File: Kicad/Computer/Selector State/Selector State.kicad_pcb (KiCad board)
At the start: 2 copper layers, 61 x 61 mm, 73 parts, among them IC1 FAN2558S38X, IC10 74LVC257AD,118, IC11 74LVC257AD,118, IC12 74LVC4245APW,118, IC2 74LVC32APW,118, IC3 74LVC32APW,118, IC4 74VHC595FT, IC5 74LVC2G08DP-Q100H, IC6 SN74ABT245BDBR, IC7 SN74ABT245BDBR, IC8 74ALVC04PW,118, IC9 74ALVC00PW,118, J1 Conn_01x02_Male, J10 Conn_01x02_Male, J11 Conn_01x10_Male, J12 Conn_01x02_Male, J2 Conn_01x12_Male, J3 Conn_01x02_Male, J4 Conn_01x02_Male, J5 Conn_01x12_Male, J6 Conn_01x02_Male, J7 Conn_01x02_Male, J8 Conn_01x10_Male, J9 Conn_01x02_Male

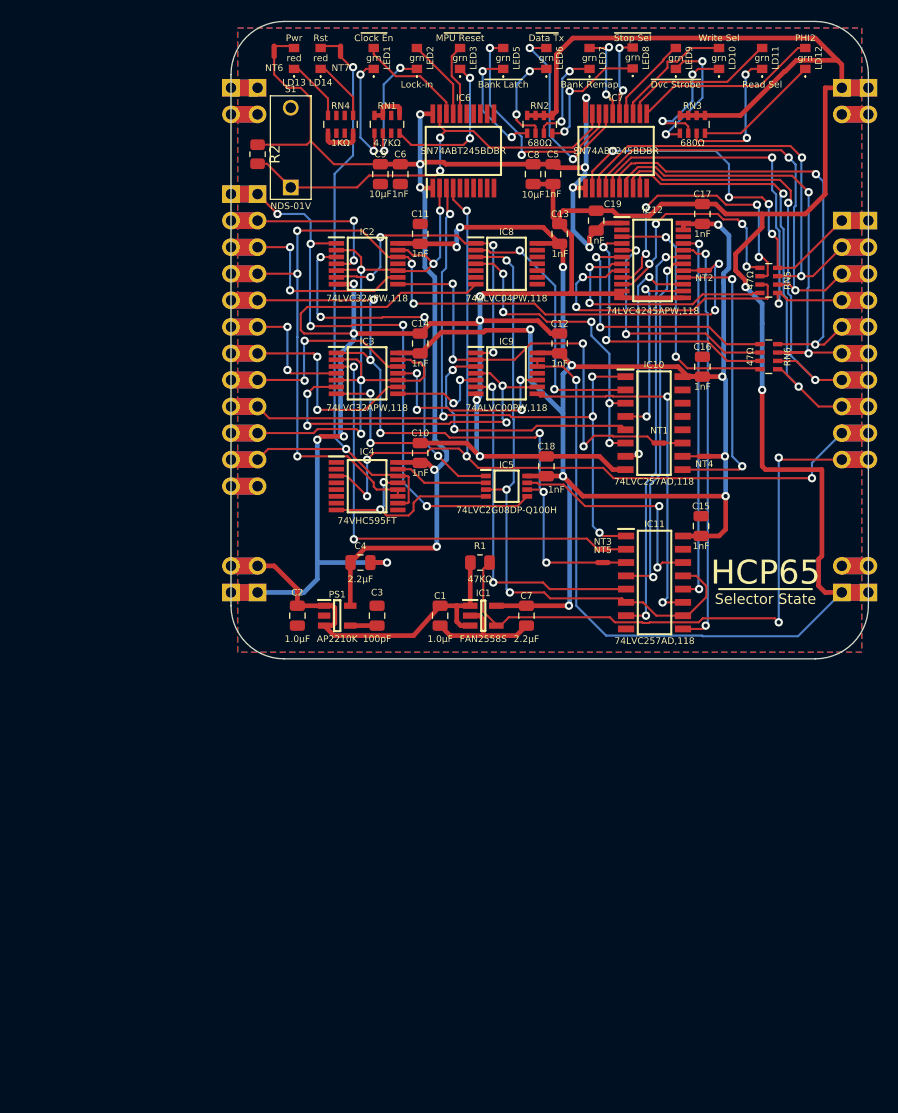
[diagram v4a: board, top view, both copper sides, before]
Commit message: Re-routed Selector State based on new simulation.
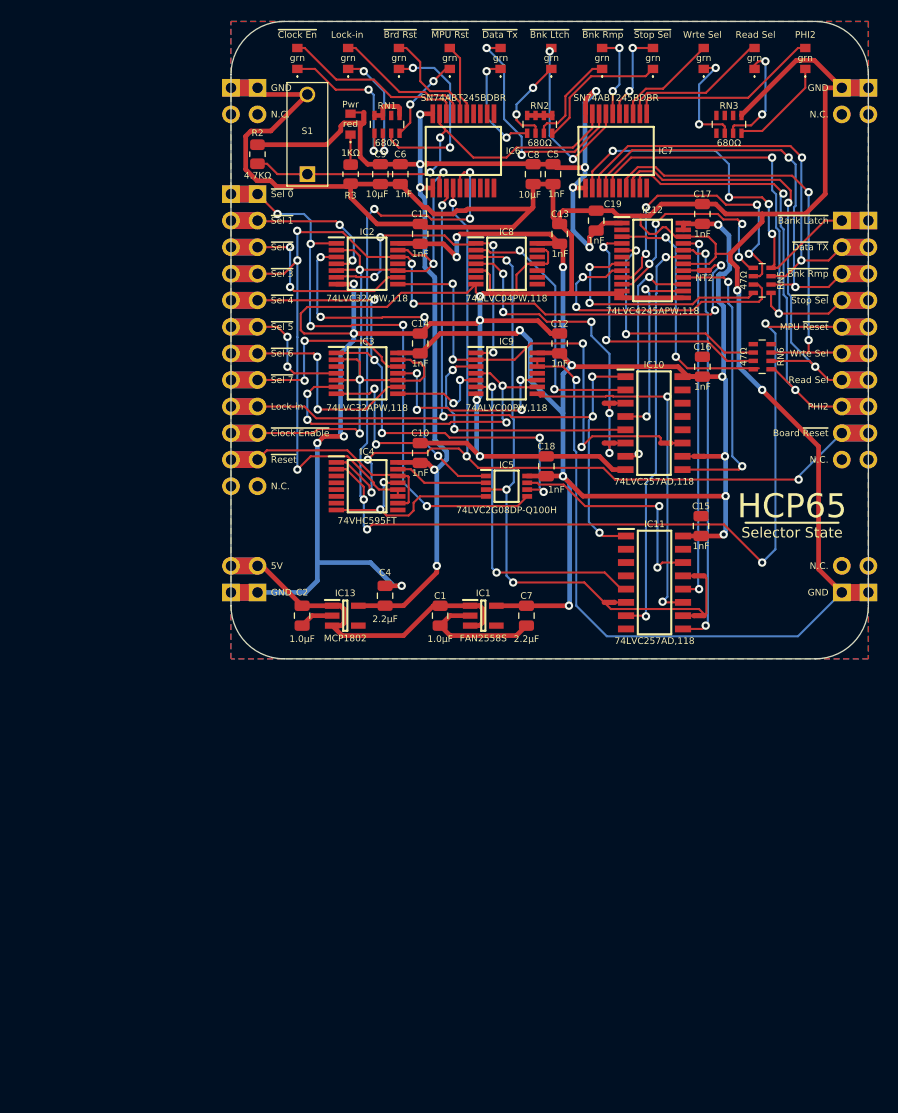
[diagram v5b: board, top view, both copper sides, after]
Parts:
- removed C3: C_Small, Capacitor_SMD:C_0805_2012Metric
- removed LD14: 150224SS73100, SamacSys_Parts:150224SS73100A
- removed LED9: 150224VS73100A, SamacSys_Parts:150224VS73100A
- removed PS1: AP2210K-5.0TRG1, SamacSys_Parts:SOT95P282X130-5N
- removed R1: R_Small, Resistor_SMD:R_0805_2012Metric
- removed RN4: CAY16-102J4LF, SamacSys_Parts:CAY16-J4
- added IC13: MCP1802T-5002I_OT, SamacSys_Parts:SOT95P270X145-5N, F.Cu at (153.2, 93.7)
- added LED4: 150224VS73100A, SamacSys_Parts:150224VS73100A, F.Cu at (163.2, 40.4)
- added NT8: NetTie_2, NetTie:NetTie-2_SMD_Pad0.5mm, F.Cu at (187.0, 93.7)
- added NT9: NetTie_2, NetTie:NetTie-2_SMD_Pad0.5mm, F.Cu at (187.0, 89.9)
- added R3: R_0805, SamacSys_Parts:R_0805, F.Cu at (153.7, 51.4)
- R2: value R_Small -> R_0805; footprint Resistor_SMD:R_0805_2012Metric -> SamacSys_Parts:R_0805
- RN1: value CAY16-472J4LF -> CAY16-681J4LF
- moved NT7 58.6 mm to (178.4, 92.4), turned to 0 degrees
- moved NT3 14.0 mm to (178.4, 73.3)
- moved NT5 11.4 mm to (178.4, 77.2)
- moved NT6 10.7 mm to (154.9, 46.0)
- moved LD13 8.29 mm to (153.7, 46.7)
- moved LED1 7.30 mm to (148.6, 40.4)
- moved LED2 6.57 mm to (153.4, 40.4)
- moved LED3 5.84 mm to (158.3, 40.4)
- moved C4 3.95 mm to (157.0, 91.8), turned to -90 degrees
- moved RN3 3.49 mm to (189.9, 46.7)
- moved S1 2.03 mm to (149.5, 51.4)
- moved LED8 1.94 mm to (182.6, 40.4)
- moved LD10 1.46 mm to (187.5, 40.4)
- moved LED7 1.21 mm to (177.7, 40.4)
- moved LD11 0.73 mm to (192.3, 40.4)
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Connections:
- net /Power LED renamed /Power^{LED}
- net 3V renamed /3.8V
- net Net-(IC6-Pad16) renamed /Board ~{Reset}^{LED}
- net Net-(IC6-Pad17) renamed /MPU Lock-in^{LED}
- net Net-(IC6-Pad18) renamed /~{Clock Enable}^{LED}
- net Net-(IC7-Pad11) renamed /~{PHI2}^{LED}
- net Net-(IC7-Pad12) renamed /Read Selector^{LED}
- net Net-(IC7-Pad13) renamed /Write Selector^{LED}
- net Net-(IC7-Pad15) renamed /~{Stop Selector}^{LED}
- net Net-(IC7-Pad16) renamed /~{Read Bank Remap}^{LED}
- net Net-(IC7-Pad17) renamed /~{Data Transmit}^{LED}
- net Net-(IC7-Pad18) renamed /~{Bank Latch}^{LED}
- C1 pad 1: GND -> /GND
- C10 pad 1: GND -> /GND
- C10 pad 2: 5V -> /5V
- C11 pad 1: GND -> /GND
- C12 pad 1: GND -> /GND
- C13 pad 1: GND -> /GND
- C14 pad 1: GND -> /GND
- C15 pad 1: GND -> /GND
- C16 pad 1: GND -> /GND
- C17 pad 1: GND -> /GND
- C18 pad 1: GND -> /GND
- C19 pad 1: GND -> /GND
- C19 pad 2: 5V -> /5V
- C2 pad 1: GND -> /GND
- C4 pad 1: GND -> /GND
- C4 pad 2: 5V -> /5V
- C5 pad 1: GND -> /GND
- C5 pad 2: 5V -> /5V
- C6 pad 1: GND -> /GND
- C6 pad 2: 5V -> /5V
- C7 pad 1: GND -> /GND
- C8 pad 1: GND -> /GND
- C8 pad 2: 5V -> /5V
- C9 pad 1: GND -> /GND
- C9 pad 2: 5V -> /5V
- IC1 pad 2: GND -> /GND
- IC1 pad 4: /~{Power Error} -> unconnected-(IC1-Pad4)
- IC10 pad 13: GND -> /GND
- IC10 pad 14: GND -> /GND
- IC10 pad 15: GND -> /GND
- IC10 pad 6: /~{Bank Latch}_{2} -> /~{Data Transmit}_{2}
- IC10 pad 8: GND -> /GND
- IC11 pad 13: /Read Selector_{2} -> /~{PHI2}_{2}
- IC11 pad 15: GND -> /GND
- IC11 pad 2: /~{Device Strobe}_{1} -> /GND
- IC11 pad 3: /~{Device Strobe}_{2} -> /GND
- IC11 pad 4: Net-(IC11-Pad4) -> unconnected-(IC11-Pad4)
- IC11 pad 6: /Read Selector_{2} -> /Write Selector_{2}
- IC11 pad 8: GND -> /GND
- IC12 pad 1: 5V -> /5V
- IC12 pad 11: GND -> /GND
- IC12 pad 12: GND -> /GND
- IC12 pad 13: GND -> /GND
- IC12 pad 18: Net-(IC11-Pad4) -> /GND
- IC12 pad 2: GND -> /GND
- IC12 pad 22: GND -> /GND
- IC12 pad 6: Net-(IC12-Pad6) -> unconnected-(IC12-Pad6)
- IC2 pad 11: /Select 3 ^{AND} Enable -> unconnected-(IC2-Pad11)
- IC2 pad 7: GND -> /GND
- IC3 pad 3: /Select 4 ^{AND} Enable -> unconnected-(IC3-Pad3)
- IC3 pad 7: GND -> /GND
- IC4 pad 1: unconnected-(IC4-Pad1) -> /Board ~{Reset}
- IC4 pad 13: GND -> /GND
- IC4 pad 16: 5V -> /5V
- IC4 pad 2: unconnected-(IC4-Pad2) -> /MPU ~{Reset}
- IC4 pad 3: /Board ~{Reset} -> unconnected-(IC4-Pad3)
- IC4 pad 8: GND -> /GND
- IC5 pad 3: /Read Selector_{2} -> Net-(IC5-Pad3)
- IC5 pad 4: GND -> /GND
- IC6 pad 1: 5V -> /5V
- IC6 pad 10: GND -> /GND
- IC6 pad 15: unconnected-(IC6-Pad15) -> /MPU ~{Reset}^{LED}
- IC6 pad 20: 5V -> /5V
- IC6 pad 5: unconnected-(IC6-Pad5) -> /MPU ~{Reset}
- IC7 pad 1: 5V -> /5V
- IC7 pad 10: GND -> /GND
- IC7 pad 14: Net-(IC7-Pad14) -> unconnected-(IC7-Pad14)
- IC7 pad 20: 5V -> /5V
- IC7 pad 6: /~{Device Strobe} -> /GND
- IC8 pad 11: unconnected-(IC8-Pad11) -> /GND
- IC8 pad 13: unconnected-(IC8-Pad13) -> /GND
- IC8 pad 3: /Read Selector_{2} -> Net-(IC5-Pad3)
- IC8 pad 4: /~{Bank Latch}_{2} -> Net-(IC8-Pad4)
- IC8 pad 5: unconnected-(IC8-Pad5) -> /GND
- IC8 pad 7: GND -> /GND
- IC8 pad 9: unconnected-(IC8-Pad9) -> /GND
- IC9 pad 12: GND -> /GND
- IC9 pad 13: GND -> /GND
- IC9 pad 7: GND -> /GND
- J1 pad 1: GND -> /GND
- J10 pad 1: GND -> /GND
- J11 pad 10: /~{Power Error} -> unconnected-(J11-Pad10)
- J11 pad 5: /~{Device Strobe} -> /MPU ~{Reset}
- J12 pad 1: GND -> /GND
- J3 pad 1: GND -> /GND
- J4 pad 1: GND -> /GND
- J4 pad 2: unconnected-(J1-Pad2) -> unconnected-(J4-Pad2)
- J5 pad 12: unconnected-(J2-Pad12) -> unconnected-(J5-Pad12)
- J6 pad 1: GND -> /GND
- J7 pad 1: GND -> /GND
- J7 pad 2: unconnected-(J10-Pad2) -> unconnected-(J7-Pad2)
- J8 pad 10: /~{Power Error} -> unconnected-(J8-Pad10)
- J8 pad 5: /~{Device Strobe} -> /MPU ~{Reset}
- J9 pad 1: GND -> /GND
- J9 pad 2: unconnected-(J12-Pad2) -> unconnected-(J9-Pad2)
- NT3 pad 1: /Select 4 ^{AND} Enable -> Net-(IC8-Pad4)
- NT3 pad 2: /~{Device Strobe}_{1} -> /~{Bank Latch}_{2}
- NT5 pad 1: /~{Select 4} -> Net-(IC8-Pad4)
- NT5 pad 2: /~{Device Strobe}_{2} -> /~{Data Transmit}_{2}
- NT6 pad 1: 5V -> /5V
- NT7 pad 1: /~{Reset} -> Net-(IC5-Pad3)
- NT7 pad 2: /Reset LED -> /Write Selector_{2}
- R2 pad 1: 5V -> /LED Enable
- R2 pad 2: /LED Enable -> /5V
- RN1 pad 3: unconnected-(RN1-Pad3) -> Net-(LED3-Pad1)
- RN1 pad 4: Net-(LED3-Pad1) -> Net-(LED4-Pad1)
- RN1 pad 5: GND -> /GND
- RN1 pad 6: unconnected-(RN1-Pad6) -> /GND
- RN1 pad 7: GND -> /GND
- RN1 pad 8: GND -> /GND
- RN2 pad 5: GND -> /GND
- RN2 pad 6: GND -> /GND
- RN2 pad 7: GND -> /GND
- RN2 pad 8: GND -> /GND
- RN3 pad 1: Net-(LED9-Pad1) -> unconnected-(RN3-Pad1)
- RN3 pad 5: GND -> /GND
- RN3 pad 6: GND -> /GND
- RN3 pad 7: GND -> /GND
- RN3 pad 8: GND -> unconnected-(RN3-Pad8)
- RN6 pad 1: Net-(IC12-Pad6) -> unconnected-(RN6-Pad1)
- RN6 pad 8: /~{Device Strobe} -> unconnected-(RN6-Pad8)
- S1 pad 2: GND -> /GND
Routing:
- net /GND: track 0.00 -> 485.5 mm, vias 0 -> 16
- net GND: track 433.9 -> 0.00 mm, vias 16 -> 0
- net 5V: track 128.1 -> 0.00 mm, vias 9 -> 0
- net /MPU ~{Reset}: track 0.00 -> 128.0 mm, vias 0 -> 7
- net /5V: track 0.00 -> 122.2 mm, vias 0 -> 9
- net /~{Power Error}: track 61.2 -> 0.00 mm, vias 2 -> 0
- net Net-(IC5-Pad3): track 0.00 -> 60.2 mm, vias 0 -> 3
- net /Read Selector_{2}: track 61.2 -> 1.03 mm, vias 3 -> 0
- net /~{Device Strobe}: track 49.8 -> 0.00 mm, vias 2 -> 0
- net /Select 4 ^{AND} Enable: track 41.9 -> 0.00 mm, vias 2 -> 0
- net /~{Reset}: track 63.7 -> 24.3 mm, vias 2 -> 0
- net Net-(IC11-Pad4): track 34.6 -> 0.00 mm, vias 2 -> 0
- net Net-(IC8-Pad4): track 0.00 -> 31.3 mm, vias 0 -> 5
- net /~{Bank Latch}_{2}: track 30.9 -> 1.03 mm, vias 5 -> 0
- net Net-(IC12-Pad6): track 25.3 -> 0.00 mm, vias 2 -> 0
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- added copper zone on B.Cu, net /GND
- added copper zone on F.Cu, net /GND
- removed copper zone on B.Cu, net GND
- removed copper zone on F.Cu, net GND
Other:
- board text added: "5V"
- board text added: "Board ~{Reset}"
- board text added: "GND"
- board text added: "MPU ~{Reset}"
- board text added: "N.C."
- board text added: "Wrte Sel"
- board text added: "~{Bank Latch}"
- board text added: "~{Bnk Ltch}"
- board text added: "~{Bnk Rmp}"
- board text added: "~{Brd Rst}"
- board text added: "~{Clock Enable}"
- board text added: "~{Clock En}"
- board text added: "~{Data TX}"
- board text added: "~{Data Tx}"
- board text added: "~{MPU Rst}"
- board text added: "~{Reset}"
- board text added: "~{Sel 0}"
- board text added: "~{Sel 1}"
- board text added: "~{Sel 2}"
- board text added: "~{Sel 3}"
- board text added: "~{Sel 4}"
- board text added: "~{Sel 5}"
- board text added: "~{Sel 6}"
- board text added: "~{Sel 7}"
- board text removed: "B~{ank Latc}h"
- board text removed: "B~{ank Rema}p"
- board text removed: "C~{lock E}n"
- board text removed: "D~{ata T}x"
- board text removed: "M~{PU Rese}t"
- board text removed: "Rst"
- board text removed: "Write Sel"
- board text removed: "~{Dvc Strobe}"

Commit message: Fixed up a bunch of clock issues.
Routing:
- net /~{PHI2}: track 48.0 -> 46.2 mm
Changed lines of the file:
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@@
     (0 "F.Cu" signal)
     (31 "B.Cu" signal)
-    (34 "B.Paste" user)
-    (35 "F.Paste" user)
     (37 "F.SilkS" user "F.Silkscreen")
     (38 "B.Mask" user)
@@
     (stackup
       (layer "F.SilkS" (type "Top Silk Screen"))
-      (layer "F.Paste" (type "Top Solder Paste"))
       (layer "F.Mask" (type "Top Solder Mask") (thickness 0.01))
       (layer "F.Cu" (type "copper") (thickness 0.035))
@@
       (layer "B.Cu" (type "copper") (thickness 0.035))
       (layer "B.Mask" (type "Bottom Solder Mask") (thickness 0.01))
-      (layer "B.Paste" (type "Bottom Solder Paste"))
       (copper_finish "None")
       (dielectric_constraints no)
@@
     (grid_origin 184.4675 40.64)
     (pcbplotparams
-      (layerselection 0x00010fc_ffffffff)
+      (layerselection 0x00010e0_ffffffff)
       (disableapertmacros false)
       (usegerberextensions false)
@@
       (outputformat 1)
       (mirror false)
-      (drillshape 1)
+      (drillshape 0)
       (scaleselection 1)
-      (outputdirectory "")
+      (outputdirectory "Fabrication/")
     )
   )
@@
     (fp_line (start -0.635 1) (end -0.635 -1) (layer "F.Fab") (width 0.1))
     (fp_line (start 0.615 -1) (end 0.615 1) (layer "F.Fab") (width 0.1))
-    (pad "1" smd roundrect (at -0.01 0.9125 90) (size 1.025 1.4) (layers "F.Cu" "F.Paste" "F.Mask") (roundrect_rratio 0.243902)
+    (pad "1" smd roundrect (at -0.01 0.9125 90) (size 1.025 1.4) (layers "F.Cu" "F.Paste" "F.Mask") (roundrect_rratio 0.243902439)
       (net 30 "/LED Enable") (pintype "passive"))
-    (pad "2" smd roundrect (at -0.01 -0.9125 90) (size 1.025 1.4) (layers "F.Cu" "F.Paste" "F.Mask") (roundrect_rratio 0.243902)
+    (pad "2" smd roundrect (at -0.01 -0.9125 90) (size 1.025 1.4) (layers "F.Cu" "F.Paste" "F.Mask") (roundrect_rratio 0.243902439)
       (net 109 "/5V") (pintype "passive"))
     (model "${KICAD6_3DMODEL_DIR}/Resistor_SMD.3dshapes/R_0805_2012Metric.wrl"
@@
     (property "Silkscreen" "47Ω")
     (attr smd)
-    (fp_text reference "RN5" (at 0 -1.778 -90) (layer "F.SilkS")
+    (fp_text reference "RN5" (at -2.2225 0) (layer "F.SilkS")
       (effects (font (size 0.635 0.635) (thickness 0.15)))
     )
@@
       (effects (font (size 0.635 0.635) (thickness 0.15)))
     )
-    (fp_text user "${Silkscreen}" (at 0 1.778 -90) (layer "F.SilkS")
+    (fp_text user "${Silkscreen}" (at 2.2225 0) (layer "F.SilkS")
       (effects (font (size 0.635 0.635) (thickness 0.15)))
     )
@@
     (fp_line (start 0.615 -1) (end 0.615 1) (layer "F.Fab") (width 0.1))
     (fp_line (start 0.615 1) (end -0.635 1) (layer "F.Fab") (width 0.1))
-    (pad "1" smd roundrect (at -0.01 0.9125 270) (size 1.025 1.4) (layers "F.Cu" "F.Paste" "F.Mask") (roundrect_rratio 0.243902)
+    (pad "1" smd roundrect (at -0.01 0.9125 270) (size 1.025 1.4) (layers "F.Cu" "F.Paste" "F.Mask") (roundrect_rratio 0.243902439)
       (net 55 "Net-(LD13-Pad1)") (pintype "passive"))
-    (pad "2" smd roundrect (at -0.01 -0.9125 270) (size 1.025 1.4) (layers "F.Cu" "F.Paste" "F.Mask") (roundrect_rratio 0.243902)
+    (pad "2" smd roundrect (at -0.01 -0.9125 270) (size 1.025 1.4) (layers "F.Cu" "F.Paste" "F.Mask") (roundrect_rratio 0.243902439)
       (net 108 "/GND") (pintype "passive"))
     (model "${KICAD6_3DMODEL_DIR}/Resistor_SMD.3dshapes/R_0805_2012Metric.wrl"
@@
     (property "Silkscreen" "47Ω")
     (attr smd)
-    (fp_text reference "RN6" (at 0 -1.778 -90) (layer "F.SilkS")
+    (fp_text reference "RN6" (at -2.2225 0) (layer "F.SilkS")
       (effects (font (size 0.635 0.635) (thickness 0.15)))
     )
@@
       (effects (font (size 0.635 0.635) (thickness 0.15)))
     )
-    (fp_text user "${Silkscreen}" (at 0 1.778 -90) (layer "F.SilkS")
+    (fp_text user "${Silkscreen}" (at 2.2225 0) (layer "F.SilkS")
       (effects (font (size 0.635 0.635) (thickness 0.15)))
     )
@@
     (property "Sheetname" "")
     (attr exclude_from_pos_files)
-    (fp_text reference "NT2" (at 0 -0.725) (layer "F.SilkS")
+    (fp_text reference "NT2" (at 0 -0.725) (layer "F.SilkS") hide
       (effects (font (size 0.635 0.635) (thickness 0.15)))
     )
-    (fp_text value "NetTie_2" (at 0 1.2) (layer "F.Fab")
+    (fp_text value "NetTie_2" (at 0 1.2) (layer "F.Fab") hide
       (effects (font (size 0.635 0.635) (thickness 0.15)))
     )
@@
   (segment (start 195.809342 63.131087) (end 195.809342 67.539342) (width 0.2) (layer "B.Cu") (net 49))
   (segment (start 195.541368 54.174699) (end 195.5155 54.200567) (width 0.2) (layer "B.Cu") (net 49))
-  (segment (start 200.66 73.66) (end 197.8025 73.66) (width 0.2) (layer "F.Cu") (net 50))
   (segment (start 182.519511 51.562989) (end 183.337056 52.380534) (width 0.2) (layer "F.Cu") (net 50))
   (segment (start 181.345 51.688478) (end 181.470489 51.562989) (width 0.2) (layer "F.Cu") (net 50))
-  (segment (start 197.8025 73.66) (end 196.215 72.0725) (width 0.2) (layer "F.Cu") (net 50))
+  (segment (start 197.1675 70.1675) (end 196.5325 70.1675) (width 0.2) (layer "F.Cu") (net 50))
   (segment (start 181.470489 51.562989) (end 182.519511 51.562989) (width 0.2) (layer "F.Cu") (net 50))
+  (segment (start 194.31 70.1675) (end 196.5325 70.1675) (width 0.2) (layer "F.Cu") (net 50))
+  (segment (start 200.66 73.66) (end 197.1675 70.1675) (width 0.2) (layer "F.Cu") (net 50))
   (segment (start 181.345 52.7625) (end 181.345 51.688478) (width 0.2) (layer "F.Cu") (net 50))
   (segment (start 203.2 73.66) (end 200.66 73.66) (width 1.6) (layer "F.Cu") (net 50))
   (segment (start 194.157252 52.380534) (end 195.070029 53.293311) (width 0.2) (layer "F.Cu") (net 50))
-  (segment (start 194.24 70.0975) (end 196.215 72.0725) (width 0.2) (layer "F.Cu") (net 50))
   (segment (start 183.337056 52.380534) (end 194.157252 52.380534) (width 0.2) (layer "F.Cu") (net 50))
-  (via (at 196.215 72.0725) (size 0.8) (drill 0.4) (layers "F.Cu" "B.Cu") (net 50))
+  (segment (start 194.24 70.0975) (end 194.31 70.1675) (width 0.2) (layer "F.Cu") (net 50))
+  (via (at 196.5325 70.1675) (size 0.8) (drill 0.4) (layers "F.Cu" "B.Cu") (net 50))
   (via (at 195.070029 53.293311) (size 0.8) (drill 0.4) (layers "F.Cu" "B.Cu") (net 50))
-  (segment (start 195.091511 56.694772) (end 195.091511 62.97825) (width 0.2) (layer "B.Cu") (net 50))
-  (segment (start 194.816 56.419261) (end 195.091511 56.694772) (width 0.2) (layer "B.Cu") (net 50))
-  (segment (start 195.091511 62.97825) (end 195.398443 63.285182) (width 0.2) (layer "B.Cu") (net 50))
-  (segment (start 195.398443 63.285182) (end 195.398443 71.255943) (width 0.2) (layer "B.Cu") (net 50))
-  (segment (start 200.66 73.66) (end 203.2 73.66) (width 1.6) (layer "B.Cu") (net 50))
   (segment (start 194.816 53.54734) (end 194.816 56.419261) (width 0.2) (layer "B.Cu") (net 50))
-  (segment (start 195.398443 71.255943) (end 196.215 72.0725) (width 0.2) (layer "B.Cu") (net 50))
+  (segment (start 200.66 73.66) (end 203.2 73.66) (width 1.6) (layer "B.Cu") (net 50))
+  (segment (start 195.091511 62.97825) (end 195.398443 63.285182) (width 0.2) (layer "B.Cu") (net 50))
   (segment (start 195.070029 53.293311) (end 194.816 53.54734) (width 0.2) (layer "B.Cu") (net 50))
+  (segment (start 195.398443 69.033443) (end 196.5325 70.1675) (width 0.2) (layer "B.Cu") (net 50))
+  (segment (start 194.816 56.419261) (end 195.091511 56.694772) (width 0.2) (layer "B.Cu") (net 50))
+  (segment (start 195.091511 56.694772) (end 195.091511 62.97825) (width 0.2) (layer "B.Cu") (net 50))
+  (segment (start 195.398443 63.285182) (end 195.398443 69.033443) (width 0.2) (layer "B.Cu") (net 50))
   (segment (start 153.67 50.5125) (end 153.67 47.6565) (width 0.2) (layer "F.Cu") (net 55))
   (segment (start 155.9625 47.5225) (end 155.9625 49.1425) (width 0.2) (layer "F.Cu") (net 56))
